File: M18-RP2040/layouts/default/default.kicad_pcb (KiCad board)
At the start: 2 copper layers, 82.5 x 39.8 mm, 70 parts

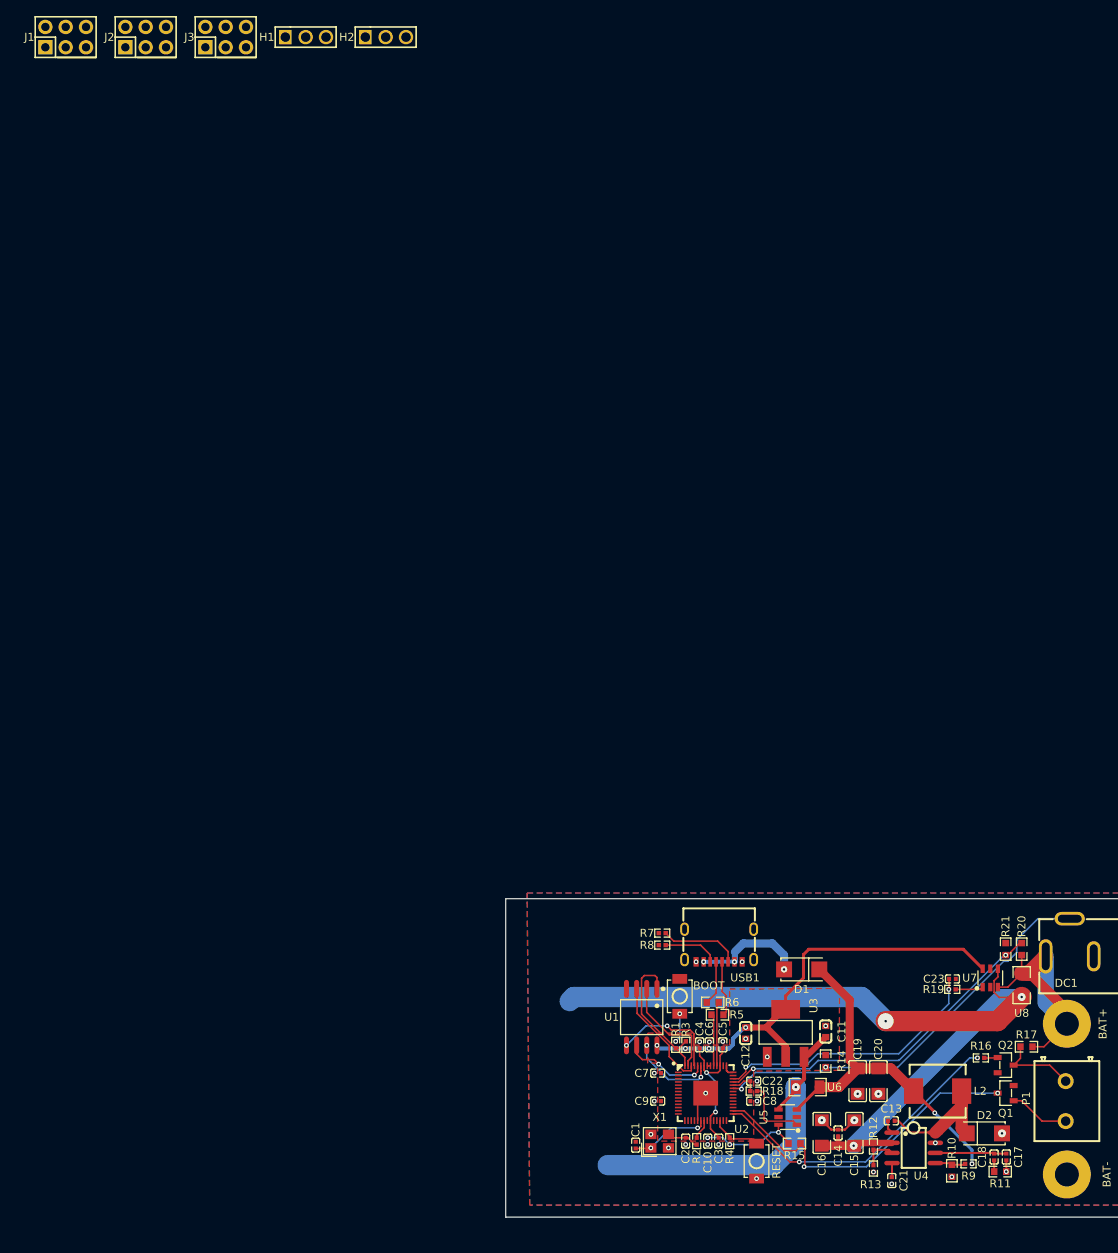
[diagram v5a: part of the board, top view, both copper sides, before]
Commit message: Fixed RP2040 board headers
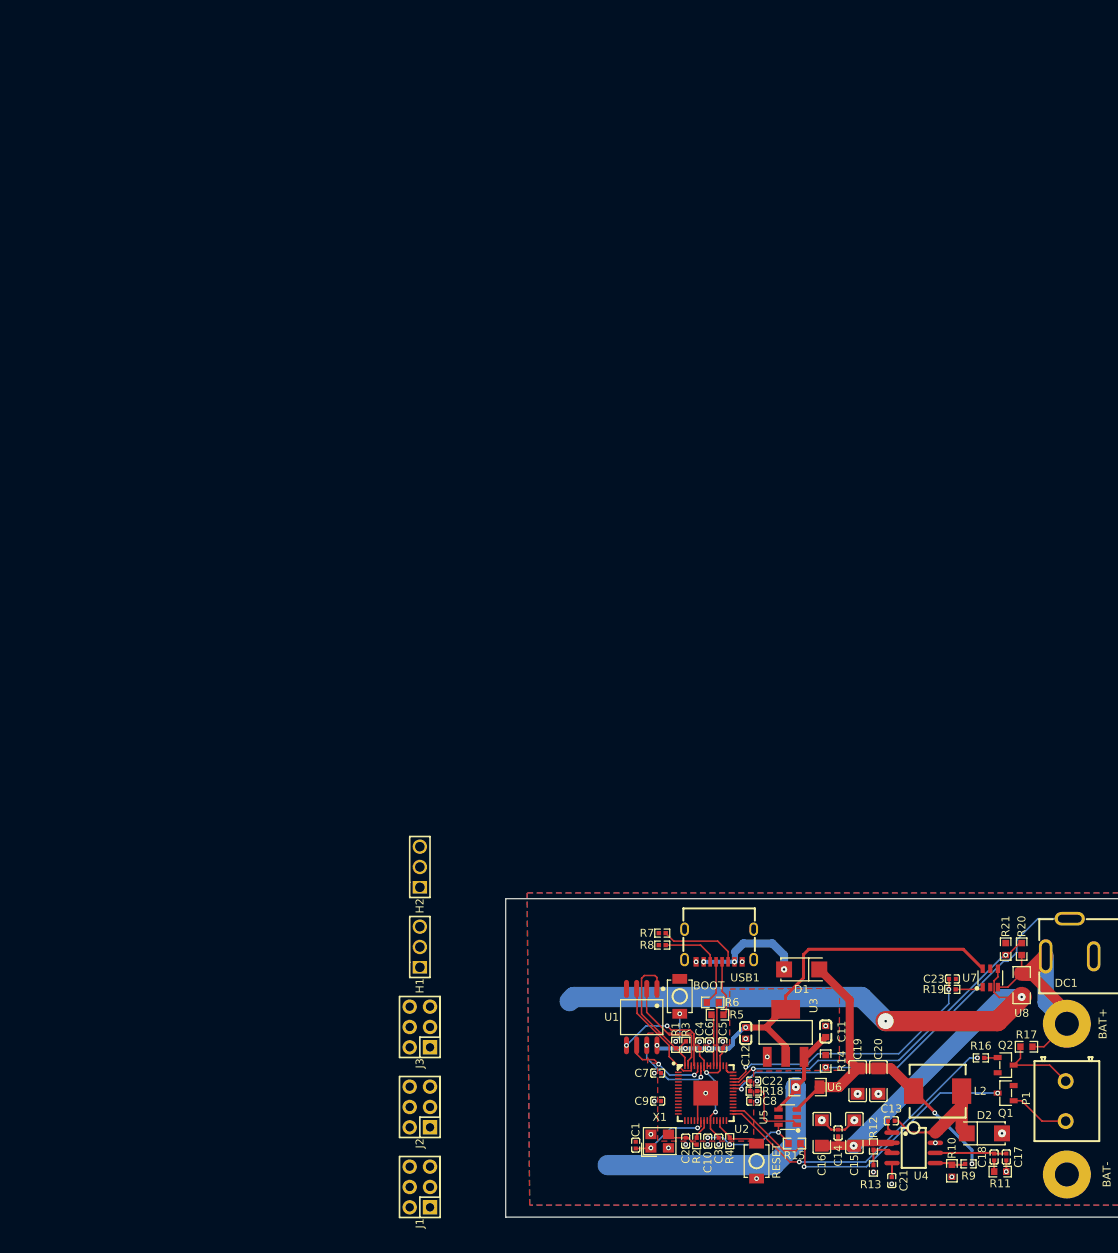
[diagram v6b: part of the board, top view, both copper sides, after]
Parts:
- moved J1 150.4 mm to (44.3, 143.7), turned to 90 degrees
- moved J2 138.1 mm to (44.3, 133.7), turned to 90 degrees
- moved J3 126.1 mm to (44.3, 123.7), turned to 90 degrees
- moved H1 114.6 mm to (44.3, 113.7), turned to 90 degrees
- moved H2 103.8 mm to (44.3, 103.7), turned to 90 degrees
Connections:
- J1 pad 2: V+ -> GND
- J1 pad 5: GND -> V+
- J2 pad 2: V+ -> GND
- J2 pad 5: GND -> V+
- J3 pad 2: V+ -> GND
- J3 pad 5: GND -> V+
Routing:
- net V+: track 0.00 -> 104.8 mm, vias 0 -> 3
- net 57: track 104.8 -> 0.00 mm, vias 3 -> 0
- net 60: track 43.2 -> 0.00 mm, vias 1 -> 0
- net 5V: track 0.00 -> 43.2 mm, vias 0 -> 1
- net EN: track 0.00 -> 4.39 mm
- net (no net): track 4.39 -> 0.00 mm

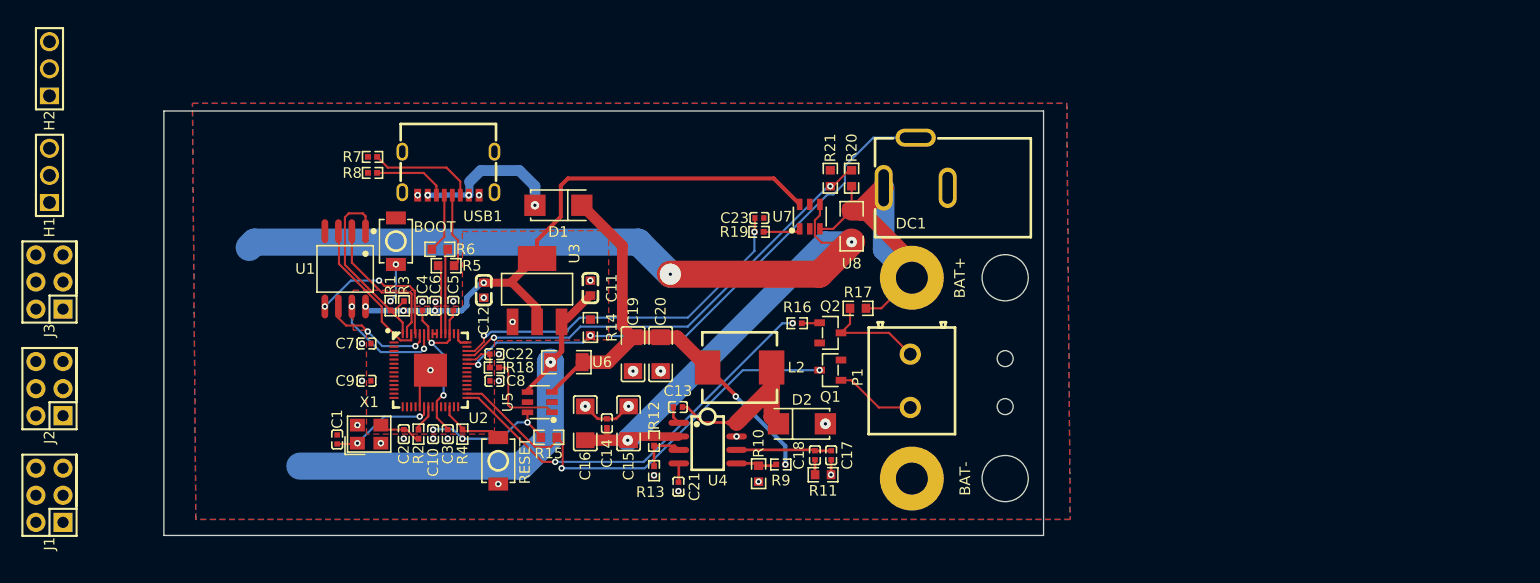
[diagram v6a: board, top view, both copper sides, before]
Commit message: Fixed and routed M18 headers
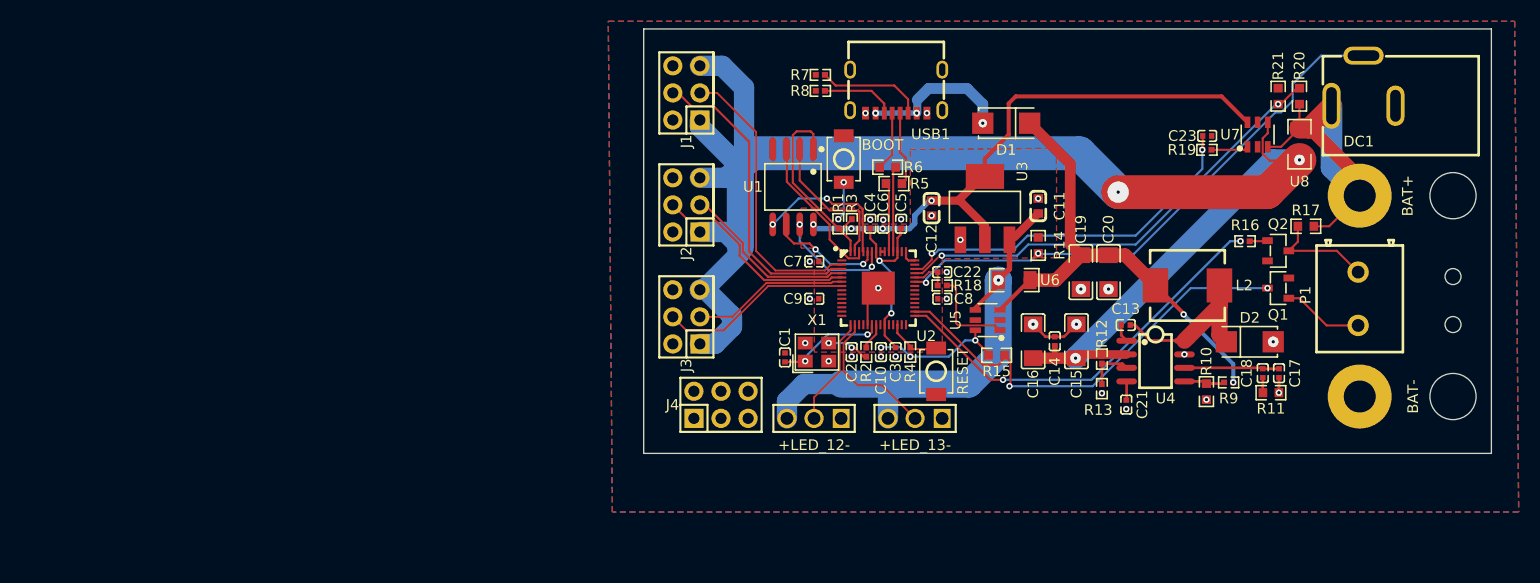
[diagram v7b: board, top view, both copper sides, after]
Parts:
- added J4: , BOOMELE_2_54_2_3P:HDR-TH_6P-P2.54-V-M-R2-C3-S2.54-1, F.Cu at (107.2, 135.2)
- C1, C2: value 20pF ±20% -> 22pF ±5%
- C10, C3, C4, C5, C6, C7, C8, C9: value 1µF ±20% -> 1µF ±10%
- C11: value 10µF ±20% -> 10µF ±10%
- C15, C16: value 4.7µF ±20% -> 4.7µF ±10%
- R1, R2: value 1kΩ ±5% -> 1kΩ ±1%
- R10: value {ℝ+}Ω -> 1.8kΩ ±1%
- R3, R4: value 10kΩ ±5% -> 10kΩ ±1%
- R5, R6: value 22Ω ±5% -> 22Ω ±1%
- R7, R8: value 5.1kΩ ±5% -> 5.1kΩ ±1%
- R9: value {ℝ+}Ω -> 10kΩ ±1%
- moved +LED_13- 84.3 mm to (125.5, 136.5), turned to 180 degrees
- moved +LED_12- 78.8 mm to (116.0, 136.5), turned to 180 degrees
- moved J1 70.6 mm to (104.0, 106.0)
- moved J2 62.2 mm to (104.0, 116.5)
- moved J3 59.8 mm to (104.0, 127.0)
- moved C16 42.7 mm to (136.5, 129.3)
- moved R10 42.7 mm to (152.8, 134.0)
- moved BAT+ 42.7 mm to (167.2, 115.6)
- moved BAT- 42.7 mm to (167.2, 134.5)
- moved BOOT 42.7 mm to (118.8, 112.2)
- moved C1 42.7 mm to (113.2, 130.8)
- moved C10 42.7 mm to (122.2, 130.3)
- moved C11 42.7 mm to (137.0, 116.6)
- moved C12 42.7 mm to (127.0, 116.8)
- moved C14 42.7 mm to (138.6, 129.3)
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- renumbered H2 to +LED_12-, H1 to +LED_13-
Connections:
- net 3-1 renamed GPIO2
- net 4 renamed GPIO1
- net 4-1 renamed GPIO3
- net RX renamed GPI54
- net TX renamed GPIO4
- +LED_12- pad 2: spi1_cs -> GPIO12
- +LED_13- pad 2: 2 -> GPIO13
- DC1 pad 3: 3-2 -> 3
- J1 pad 3: 3 -> GPIO0
- R14 pad 1: 3-2 -> 3
- U2 pad 15: gpio12 -> GPIO12
- U2 pad 16: gpio13 -> GPIO13
- U2 pad 2: 3 -> GPIO0
- U2 pad 37: 3-2 -> 3
- U2 pad 8: 2 -> gpio6
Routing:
- net 3-2: track 52.1 -> 0.00 mm, vias 2 -> 0
- net 3: track 0.00 -> 52.1 mm, vias 0 -> 2
- net V+: track 104.8 -> 149.7 mm
- net GPIO1: track 0.00 -> 29.1 mm
- net GPIO0: track 0.00 -> 27.0 mm
- net GPIO3: track 0.00 -> 19.5 mm
- net GPI54: track 0.00 -> 18.1 mm
- net GPIO2: track 0.00 -> 16.7 mm
- net GPIO4: track 0.00 -> 14.7 mm
- net GPIO13: track 0.00 -> 13.3 mm
- net GPIO12: track 0.00 -> 10.2 mm
- net 5V: track 43.2 -> 45.5 mm
- net RUN: track 6.32 -> 5.24 mm
- net c_osc_2-power-hv: track 4.06 -> 4.66 mm, vias 0 -> 2
- net GND: vias 29 -> 28
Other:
- board size 82.5 x 39.8 mm -> 79.5 x 39.8 mm
